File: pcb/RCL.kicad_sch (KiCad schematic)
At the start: 86 parts, among them J1 USB_C_Receptacle, J2 Conn_01x02_Pin, J3 Conn_01x05_Pin, Q1 BSP613, Q2 AO3416A, Q3 AO3416A, Q4 AO3416A, SW1 SW_SPDT, SW2 SW_DIP_x02, SW3 SW_Push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

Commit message: Add missing vendor(id)
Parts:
- J2: Vendor HTL -> HTL, DigiKey; VendorId 103599 -> 103599, BC2AAAW-ND, 455-2266-ND, BXH-001T-P0.6-ND
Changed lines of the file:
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@@
 			)
 		)
-		(property "Vendor" "HTL"
+		(property "Vendor" "HTL, DigiKey"
 			(at 124.46 62.23 0)
 			(effects
@@
 			)
 		)
-		(property "VendorId" "103599"
+		(property "VendorId" "103599, BC2AAAW-ND, 455-2266-ND, BXH-001T-P0.6-ND"
 			(at 124.46 62.23 0)
 			(effects

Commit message: Rename/Add/Remove bom fields
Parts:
- C1, C5, C6, C8: HTL (none) -> 100140; Vendor HTL -> (none); VendorId 100140 -> (none)
- C10, C11, C12, C13, C14, C15, C16, C17, C18, C19, C2, C20, C4, C7, C9: HTL (none) -> 100128; Vendor HTL -> (none); VendorId 100128 -> (none)
- C3: HTL (none) -> 103620; Vendor HTL -> (none); VendorId 103620 -> (none)
- D1: HTL (none) -> 103360; Vendor HTL -> (none); VendorId 103360 -> (none)
- D10, D11, D12, D13, D14, D15, D16, D17: HTL (none) -> 103607; Vendor HTL -> (none); VendorId 103607 -> (none)
- D2: HTL (none) -> 100194; Vendor HTL -> (none); VendorId 100194 -> (none)
- D3, D7, D9: HTL (none) -> 100458; Vendor HTL -> (none); VendorId 100458 -> (none)
- D6: HTL (none) -> 100206; Vendor HTL -> (none); VendorId 100206 -> (none)
- D8: HTL (none) -> 100459; Vendor HTL -> (none); VendorId 100459 -> (none)
- F1: HTL (none) -> 103597; Vendor HTL -> (none); VendorId 103597 -> (none)
- F2: HTL (none) -> 103598; Vendor HTL -> (none); VendorId 103598 -> (none)
- FB1: HTL (none) -> 103570; Vendor HTL -> (none); VendorId 103570 -> (none)
- FID1, FID2, FID3, FID4: now left out of the parts list
- H1: HTL (none) -> 101017, 101382; Vendor HTL -> (none); VendorId 101017, 101382 -> (none)
- J1: HTL (none) -> 103572; Vendor HTL -> (none); VendorId 103572 -> (none)
- J2: DigiKey (none) -> BC2AAAW-ND, 455-2266-ND, BXH-001T-P0.6-ND; HTL (none) -> 103599; Vendor HTL, DigiKey -> (none); VendorId 103599, BC2AAAW-ND, 455-2266-ND, BXH-001T-P0.6-ND -> (none)
- J3: HTL (none) -> 101546; Vendor HTL -> (none); VendorId 101546 -> (none)
- L1: HTL (none) -> 103600; Vendor HTL -> (none); VendorId 103600 -> (none)
- Q1: HTL (none) -> 103601; Vendor HTL -> (none); VendorId 103601 -> (none)
- Q2, Q3, Q4: HTL (none) -> 103512; Vendor HTL -> (none); VendorId 103512 -> (none)
- R1, R2: HTL (none) -> 102962; Vendor HTL -> (none); VendorId 102962 -> (none)
- R13, R14: HTL (none) -> 102959; Vendor HTL -> (none); VendorId 102959 -> (none)
- R15, R17, R23, R4, R5, R6: HTL (none) -> 102951; Vendor HTL -> (none); VendorId 102951 -> (none)
- R16, R25, R26, R9: HTL (none) -> 102944; Vendor HTL -> (none); VendorId 102944 -> (none)
- R18, R7: HTL (none) -> 102967; Vendor HTL -> (none); VendorId 102967 -> (none)
- R20, R22: HTL (none) -> 102973; Vendor HTL -> (none); VendorId 102973 -> (none)
- R21, R24: DigiKey (none) -> RMCF0603ZT0R00CT-ND; Vendor DigiKey -> (none); VendorId RMCF0603ZT0R00CT-ND -> (none)
- R27: HTL (none) -> 102940; Vendor HTL -> (none); VendorId 102940 -> (none)
- R3: HTL (none) -> 103602; Vendor HTL -> (none); VendorId 103602 -> (none)
- R8: HTL (none) -> 102987; Vendor HTL -> (none); VendorId 102987 -> (none)
- SW1: HTL (none) -> 103603; Vendor HTL -> (none); VendorId 103603 -> (none)
- SW2: HTL (none) -> 103604; Vendor HTL -> (none); VendorId 103604 -> (none)
- SW3: HTL (none) -> 101612; Vendor HTL -> (none); VendorId 101612 -> (none)
- U1: HTL (none) -> 103605; Vendor HTL -> (none); VendorId 103605 -> (none)
- U2: HTL (none) -> 103606; Vendor HTL -> (none); VendorId 103606 -> (none)
- U3: HTL (none) -> 103616; Vendor HTL -> (none); VendorId 103616 -> (none)
- U4: HTL (none) -> 103615; Vendor HTL -> (none); VendorId 103615 -> (none)
- U5: DigiKey (none) -> 150-MCP2221AT-I/SLCT-ND; Vendor DigiKey -> (none); VendorId 150-MCP2221AT-I/SLCT-ND -> (none)

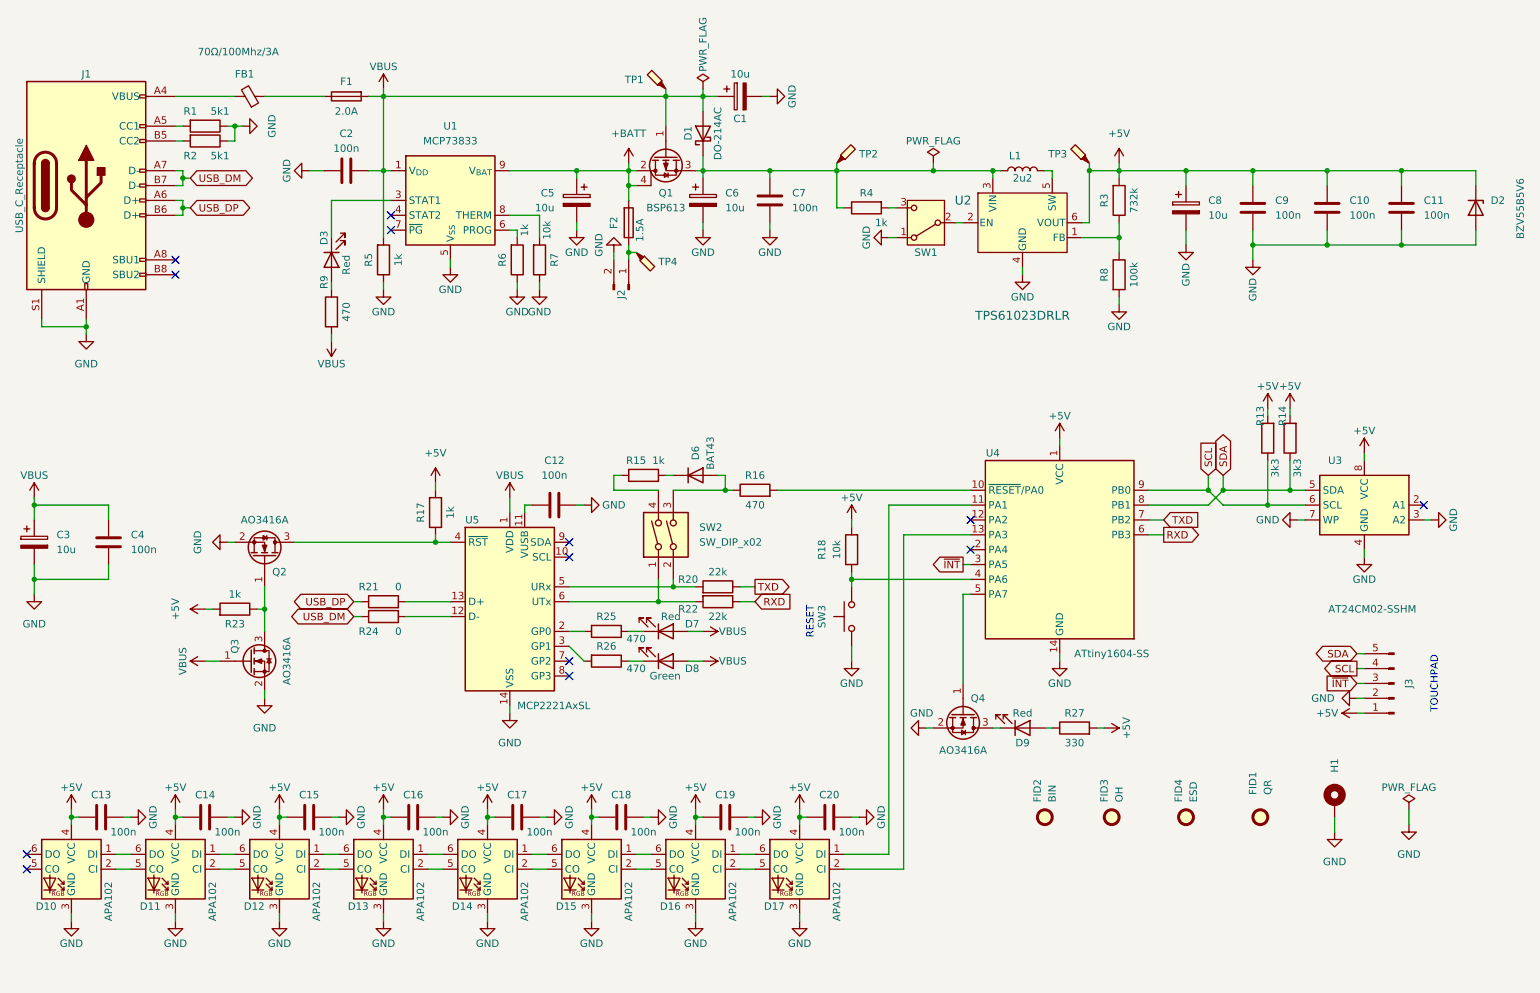
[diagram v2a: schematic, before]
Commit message: Change MCP2221A to FT230X
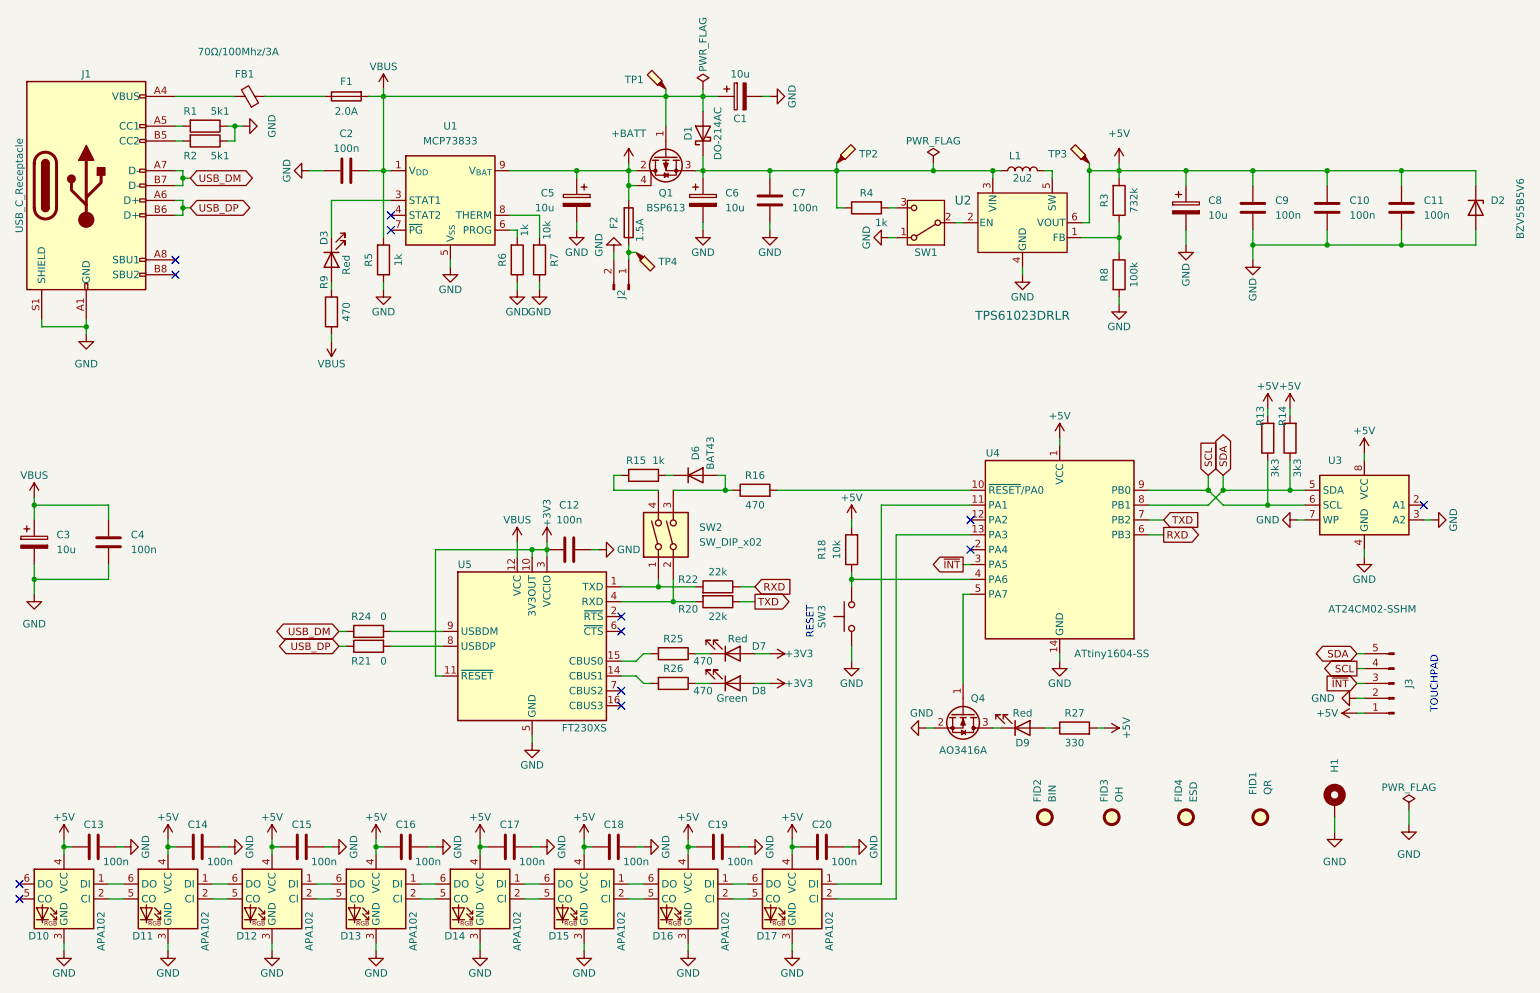
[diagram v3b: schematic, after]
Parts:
- removed Q2, Q3: AO3416A, Package_TO_SOT_SMD:SOT-23, symbol Transistor_FET:AO3400A
- removed R17, R23: 1k, Resistor_SMD:R_1206_3216Metric, symbol Device:R
- removed U5: MCP2221AxSL, Package_SO:SOIC-14_3.9x8.7mm_P1.27mm, symbol Interface_USB:MCP2221AxSL
- added U5: FT230XS, Package_SO:SSOP-16_3.9x4.9mm_P0.635mm, symbol Interface_USB:FT230XS
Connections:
- net GND: now also U5.13 (GND), U5.5 (GND)
- net VBUS: now also U5.12 (VCC); no longer D7.2 (A), D8.2 (A)
- net +3V3: now reaches C12.1
- net +3V3: now also D7.2 (A), D8.2 (A), U5.10 (3V3OUT), U5.11 (~{RESET}), U5.3 (VCCIO)
- net at R24.2: now also U5.9 (USBDM)
- net at R21.2: now also U5.8 (USBDP)
- net at R25.2: now also U5.15 (CBUS0)
- net at R26.2: now also U5.14 (CBUS1)
- net at R20.2, SW2.2: now also U5.4 (RXD)
- net at R22.2, SW2.1: now also U5.1 (TXD)
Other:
- moved on the sheet: C12, C13, C14, C15, C16, C17, C18, C19, C20, D10, D11, D12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

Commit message: Optimize +3V3 signal
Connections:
- net +3V3: no longer names the net of C12.1, D7.2 (A), D8.2 (A), U5.10 (3V3OUT), U5.11 (~{RESET}), U5.3 (VCCIO)
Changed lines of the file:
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@@
 	)
 	(junction
+		(at 91.44 128.27)
+		(diameter 0)
+		(color 0 0 0 0)
+	)
+	(junction
 		(at 48.26 43.18)
 		(diameter 0)
@@
 	)
 	(junction
+		(at 148.59 129.54)
+		(diameter 0)
+		(color 0 0 0 0)
+	)
+	(junction
 		(at 237.49 96.52)
 		(diameter 0)
@@
 	(wire
 		(pts
+			(xy 91.44 144.78) (xy 148.59 144.78)
+		)
+		(stroke
+			(width 0)
+			(type default)
+		)
+	)
+	(wire
+		(pts
 			(xy 46.99 34.29) (xy 48.26 34.29)
 		)
@@
 	(wire
 		(pts
-			(xy 208.28 63.5) (xy 208.28 64.77)
+			(xy 148.59 124.46) (xy 148.59 129.54)
 		)
 		(stroke
@@
 	(wire
 		(pts
-			(xy 55.88 34.29) (xy 57.15 34.29)
+			(xy 208.28 63.5) (xy 208.28 64.77)
 		)
 		(stroke
@@
 	(wire
 		(pts
-			(xy 110.49 105.41) (xy 110.49 106.68)
+			(xy 55.88 34.29) (xy 57.15 34.29)
 		)
 		(stroke
@@
 	(wire
 		(pts
+			(xy 148.59 129.54) (xy 148.59 144.78)
+		)
+		(stroke
+			(width 0)
+			(type default)
+		)
+	)
+	(wire
+		(pts
 			(xy 123.19 113.03) (xy 129.54 113.03)
 		)
@@
 	(wire
 		(pts
+			(xy 91.44 128.27) (xy 91.44 144.78)
+		)
+		(stroke
+			(width 0)
+			(type default)
+		)
+	)
+	(wire
+		(pts
 			(xy 147.32 29.21) (xy 148.59 29.21)
 		)
@@
 	)
 	(symbol
-		(lib_id "power:+3V3")
-		(at 148.59 124.46 270)
-		(unit 1)
-		(exclude_from_sim no)
-		(in_bom yes)
-		(on_board yes)
-		(dnp no)
-		(property "Reference" "#PWR032"
-			(at 144.78 124.46 0)
-			(effects
-				(font
-					(size 1.27 1.27)
-				)
-				(hide yes)
-			)
-		)
-		(property "Value" "+3V3"
-			(at 151.13 124.46 90)
-			(effects
-				(font
-					(size 1.27 1.27)
-				)
-				(justify left)
-			)
-		)
-		(property "Footprint" ""
-			(at 148.59 124.46 0)
-			(effects
-				(font
-					(size 1.27 1.27)
-				)
-				(hide yes)
-			)
-		)
-		(property "Datasheet" ""
-			(at 148.59 124.46 0)
-			(effects
-				(font
-					(size 1.27 1.27)
-				)
-				(hide yes)
-			)
-		)
-		(property "Description" "Power symbol creates a global label with name \"+3V3\""
-			(at 148.59 124.46 0)
-			(effects
-				(font
-					(size 1.27 1.27)
-				)
-				(hide yes)
-			)
-		)
-		(pin "1"
-		)
-		(instances
-			(project "RCL"
-				(path "/e63e39d7-6ac0-4ffd-8aa3-1841a4541b55"
-					(reference "#PWR032")
-					(unit 1)
-				)
-			)
-		)
-	)
-	(symbol
 		(lib_id "LED:APA102")
 		(at 99.06 166.37 0)
@@
 	)
 	(symbol
-		(lib_id "power:+3V3")
-		(at 148.59 129.54 270)
-		(unit 1)
-		(exclude_from_sim no)
-		(in_bom yes)
-		(on_board yes)
-		(dnp no)
-		(property "Reference" "#PWR033"
-			(at 144.78 129.54 0)
-			(effects
-				(font
-					(size 1.27 1.27)
-				)
-				(hide yes)
-			)
-		)
-		(property "Value" "+3V3"
-			(at 151.13 129.54 90)
-			(effects
-				(font
-					(size 1.27 1.27)
-				)
-				(justify left)
-			)
-		)
-		(property "Footprint" ""
-			(at 148.59 129.54 0)
-			(effects
-				(font
-					(size 1.27 1.27)
-				)
-				(hide yes)
-			)
-		)
-		(property "Datasheet" ""
-			(at 148.59 129.54 0)
-			(effects
-				(font
-					(size 1.27 1.27)
-				)
-				(hide yes)
-			)
-		)
-		(property "Description" "Power symbol creates a global label with name \"+3V3\""
-			(at 148.59 129.54 0)
-			(effects
-				(font
-					(size 1.27 1.27)
-				)
-				(hide yes)
-			)
-		)
-		(pin "1"
-		)
-		(instances
-			(project "RCL"
-				(path "/e63e39d7-6ac0-4ffd-8aa3-1841a4541b55"
-					(reference "#PWR033")
-					(unit 1)
-				)
-			)
-		)
-	)
-	(symbol
 		(lib_id "Battery_Management:MCP73833-xxx-UN")
 		(at 93.98 46.99 0)
@@
 					(unit 1)
 				)
-			)
-		)
-	)
-	(symbol
-		(lib_id "power:+3V3")
-		(at 110.49 105.41 0)
-		(unit 1)
-		(exclude_from_sim no)
-		(in_bom yes)
-		(on_board yes)
-		(dnp no)
-		(property "Reference" "#PWR025"
-			(at 110.49 109.22 0)
-			(effects
-				(font
-					(size 1.27 1.27)
-				)
-				(hide yes)
-			)
-		)
-		(property "Value" "+3V3"
-			(at 110.49 102.87 90)
-			(effects
-				(font
-					(size 1.27 1.27)
-				)
-				(justify left)
-			)
-		)
-		(property "Footprint" ""
-			(at 110.49 105.41 0)
-			(effects
-				(font
-					(size 1.27 1.27)
-				)
-				(hide yes)
-			)
-		)
-		(property "Datasheet" ""
-			(at 110.49 105.41 0)
-			(effects
-				(font
-					(size 1.27 1.27)
-				)
-				(hide yes)
-			)
-		)
-		(property "Description" "Power symbol creates a global label with name \"+3V3\""
-			(at 110.49 105.41 0)
-			(effects
-				(font
-					(size 1.27 1.27)
-				)
-				(hide yes)
-			)
-		)
-		(pin "1"
-		)
-		(instances
-			(project "RCL"
-				(path "/e63e39d7-6ac0-4ffd-8aa3-1841a4541b55"
-					(reference "#PWR025")
-					(unit 1)
-				)
